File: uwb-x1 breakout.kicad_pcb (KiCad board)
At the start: 2 copper layers, 36.5 x 28 mm, 2 parts, among them J1 Conn_01x12, U1 UWB-X1-PRO

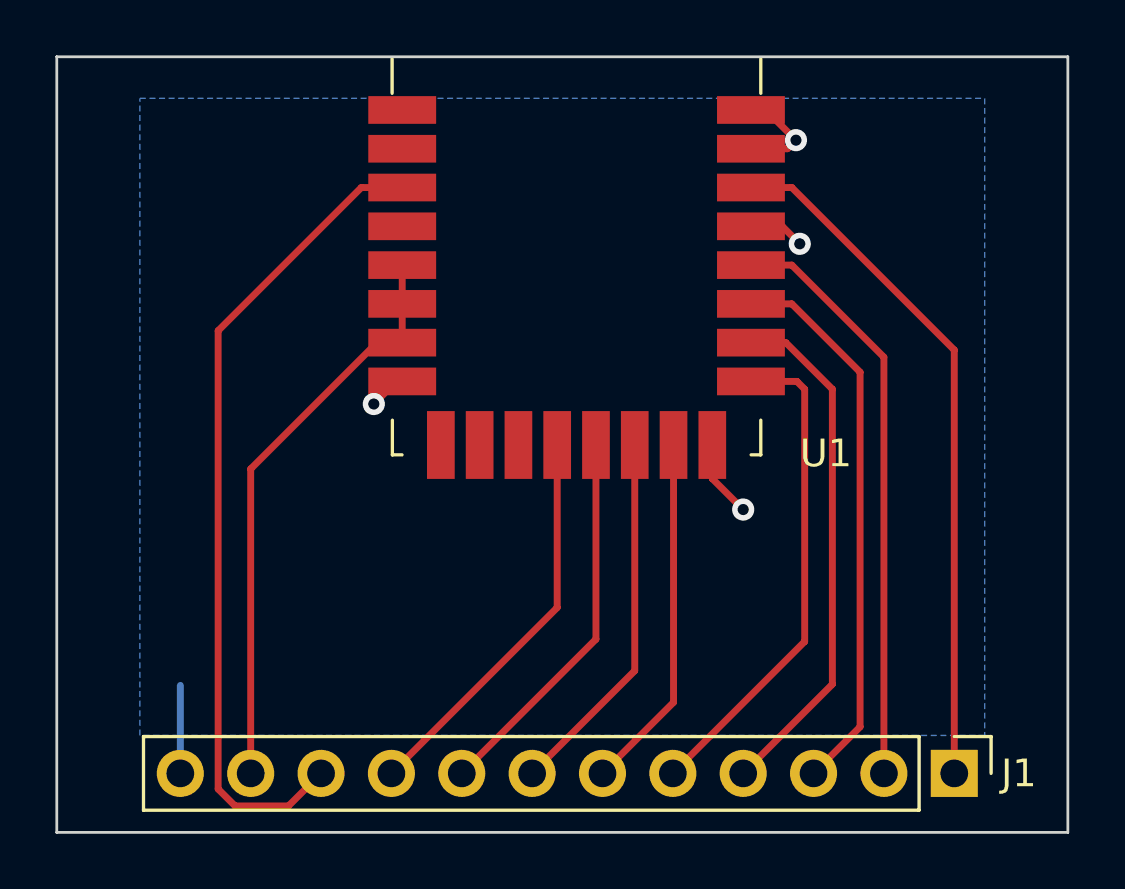
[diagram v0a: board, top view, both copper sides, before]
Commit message: Add silkscreen labels to pins
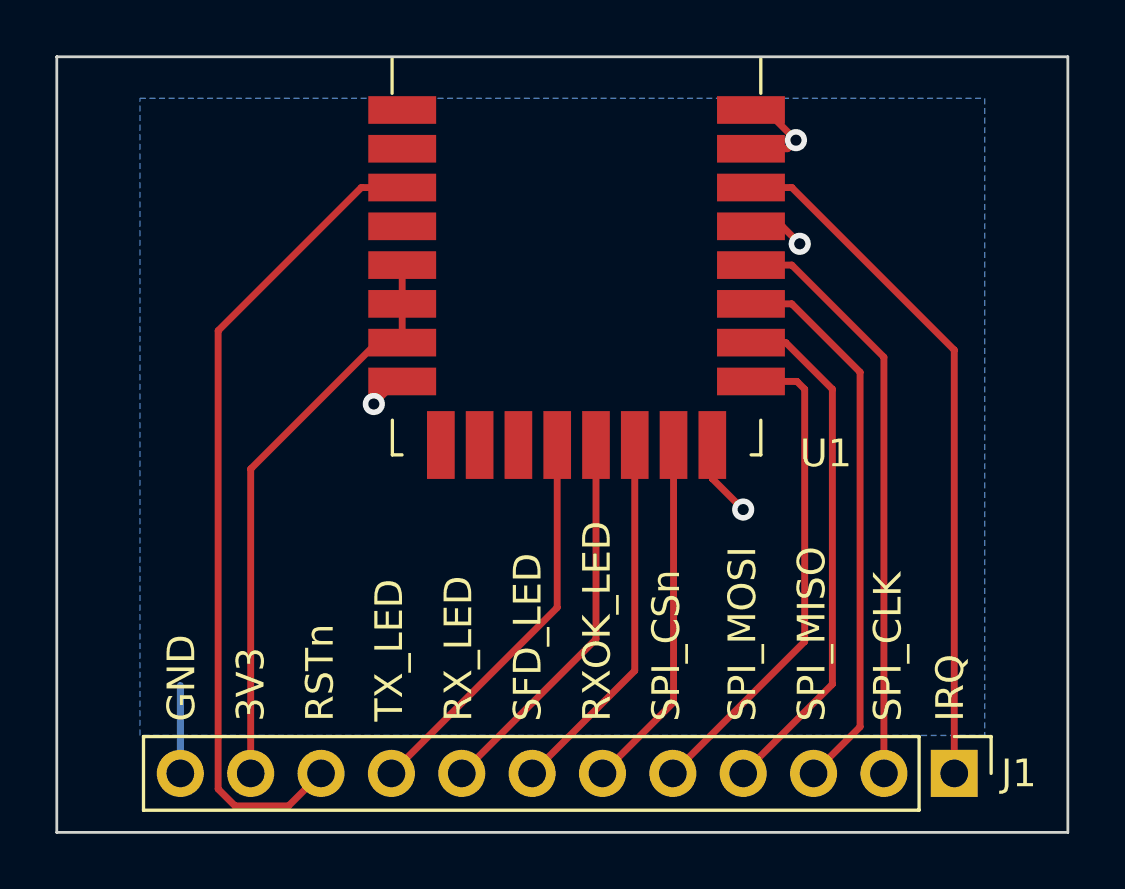
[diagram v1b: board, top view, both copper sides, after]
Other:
- board text added: "3V3"
- board text added: "GND"
- board text added: "IRQ"
- board text added: "RSTn"
- board text added: "RXOK_LED"
- board text added: "RX_LED"
- board text added: "SFD_LED"
- board text added: "SPI_CLK"
- board text added: "SPI_CSn"
- board text added: "SPI_MISO"
- board text added: "SPI_MOSI"
- board text added: "TX_LED"
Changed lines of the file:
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@@
   (general
     (thickness 1.6)
-    (drawings 4)
+    (drawings 16)
     (tracks 51)
     (zones 0)
@@
       (outputformat 1)
       (mirror false)
-      (drillshape 1)
+      (drillshape 0)
       (scaleselection 1)
-      (outputdirectory ""))
+      (outputdirectory "outputs/"))
   )
   (net 0 "")
@@
       (effects (font (size 1 1) (thickness 0.15)))
     )
+    (fp_line (start -0.635 -1.27) (end 1.27 -1.27) (layer F.Fab) (width 0.1))
+    (fp_line (start 1.27 -1.27) (end 1.27 29.21) (layer F.Fab) (width 0.1))
+    (fp_line (start 1.27 29.21) (end -1.27 29.21) (layer F.Fab) (width 0.1))
+    (fp_line (start -1.27 29.21) (end -1.27 -0.635) (layer F.Fab) (width 0.1))
+    (fp_line (start -1.27 -0.635) (end -0.635 -1.27) (layer F.Fab) (width 0.1))
+    (fp_line (start -1.33 29.27) (end 1.33 29.27) (layer F.SilkS) (width 0.12))
+    (fp_line (start -1.33 1.27) (end -1.33 29.27) (layer F.SilkS) (width 0.12))
+    (fp_line (start 1.33 1.27) (end 1.33 29.27) (layer F.SilkS) (width 0.12))
+    (fp_line (start -1.33 1.27) (end 1.33 1.27) (layer F.SilkS) (width 0.12))
+    (fp_line (start -1.33 0) (end -1.33 -1.33) (layer F.SilkS) (width 0.12))
+    (fp_line (start -1.33 -1.33) (end 0 -1.33) (layer F.SilkS) (width 0.12))
+    (fp_line (start -1.8 -1.8) (end -1.8 29.75) (layer F.CrtYd) (width 0.05))
+    (fp_line (start -1.8 29.75) (end 1.8 29.75) (layer F.CrtYd) (width 0.05))
+    (fp_line (start 1.8 29.75) (end 1.8 -1.8) (layer F.CrtYd) (width 0.05))
     (fp_line (start 1.8 -1.8) (end -1.8 -1.8) (layer F.CrtYd) (width 0.05))
-    (fp_line (start 1.8 29.75) (end 1.8 -1.8) (layer F.CrtYd) (width 0.05))
-    (fp_line (start -1.8 29.75) (end 1.8 29.75) (layer F.CrtYd) (width 0.05))
-    (fp_line (start -1.8 -1.8) (end -1.8 29.75) (layer F.CrtYd) (width 0.05))
-    (fp_line (start -1.33 -1.33) (end 0 -1.33) (layer F.SilkS) (width 0.12))
-    (fp_line (start -1.33 0) (end -1.33 -1.33) (layer F.SilkS) (width 0.12))
-    (fp_line (start -1.33 1.27) (end 1.33 1.27) (layer F.SilkS) (width 0.12))
-    (fp_line (start 1.33 1.27) (end 1.33 29.27) (layer F.SilkS) (width 0.12))
-    (fp_line (start -1.33 1.27) (end -1.33 29.27) (layer F.SilkS) (width 0.12))
-    (fp_line (start -1.33 29.27) (end 1.33 29.27) (layer F.SilkS) (width 0.12))
-    (fp_line (start -1.27 -0.635) (end -0.635 -1.27) (layer F.Fab) (width 0.1))
-    (fp_line (start -1.27 29.21) (end -1.27 -0.635) (layer F.Fab) (width 0.1))
-    (fp_line (start 1.27 29.21) (end -1.27 29.21) (layer F.Fab) (width 0.1))
-    (fp_line (start 1.27 -1.27) (end 1.27 29.21) (layer F.Fab) (width 0.1))
-    (fp_line (start -0.635 -1.27) (end 1.27 -1.27) (layer F.Fab) (width 0.1))
     (fp_text user %R (at 0 13.97) (layer F.Fab)
       (effects (font (size 1 1) (thickness 0.15)))
@@
       (effects (font (size 1 1) (thickness 0.15)))
     )
+    (fp_line (start -6.5 -5.525) (end -6.5 7.4) (layer F.Fab) (width 0.1))
+    (fp_line (start -6.5 7.4) (end 6.5 7.4) (layer F.Fab) (width 0.1))
+    (fp_line (start 6.5 7.4) (end 6.5 -5.525) (layer F.Fab) (width 0.1))
+    (fp_line (start -6.66 -6.75) (end -6.66 -5.5) (layer F.SilkS) (width 0.12))
+    (fp_line (start 6.65 -6.75) (end 6.65 -5.5) (layer F.SilkS) (width 0.12))
+    (fp_line (start -6.3 7.55) (end -6.65 7.55) (layer F.SilkS) (width 0.12))
+    (fp_line (start -6.65 7.55) (end -6.65 6.3) (layer F.SilkS) (width 0.12))
+    (fp_line (start 6.3 7.55) (end 6.65 7.55) (layer F.SilkS) (width 0.12))
+    (fp_line (start 6.65 7.55) (end 6.65 6.3) (layer F.SilkS) (width 0.12))
+    (fp_line (start 7.75 -5.525) (end 7.75 8.65) (layer F.CrtYd) (width 0.05))
+    (fp_line (start 7.75 8.65) (end -7.75 8.65) (layer F.CrtYd) (width 0.05))
+    (fp_line (start -7.75 8.65) (end -7.75 -5.525) (layer F.CrtYd) (width 0.05))
+    (fp_line (start -6.5 -5.525) (end 6.5 -5.525) (layer F.Fab) (width 0.1))
+    (fp_line (start -6.5 -5.525) (end -6.5 -15.6) (layer F.Fab) (width 0.1))
+    (fp_line (start 6.5 -5.525) (end 6.5 -15.6) (layer F.Fab) (width 0.1))
+    (fp_line (start -6.5 -15.6) (end 6.5 -15.6) (layer F.Fab) (width 0.12))
+    (fp_line (start -16.5 -5.525) (end -7.75 -5.525) (layer F.CrtYd) (width 0.05))
+    (fp_line (start 7.75 -5.525) (end 16.5 -5.525) (layer F.CrtYd) (width 0.05))
+    (fp_line (start 16.5 -5.525) (end 16.5 -15.6) (layer F.CrtYd) (width 0.05))
+    (fp_line (start 16.5 -15.6) (end -16.5 -15.6) (layer F.CrtYd) (width 0.05))
     (fp_line (start -16.5 -5.525) (end -16.5 -15.6) (layer F.CrtYd) (width 0.05))
-    (fp_line (start 16.5 -15.6) (end -16.5 -15.6) (layer F.CrtYd) (width 0.05))
-    (fp_line (start 16.5 -5.525) (end 16.5 -15.6) (layer F.CrtYd) (width 0.05))
-    (fp_line (start 7.75 -5.525) (end 16.5 -5.525) (layer F.CrtYd) (width 0.05))
-    (fp_line (start -16.5 -5.525) (end -7.75 -5.525) (layer F.CrtYd) (width 0.05))
-    (fp_line (start -6.5 -15.6) (end 6.5 -15.6) (layer F.Fab) (width 0.12))
-    (fp_line (start 6.5 -5.525) (end 6.5 -15.6) (layer F.Fab) (width 0.1))
-    (fp_line (start -6.5 -5.525) (end -6.5 -15.6) (layer F.Fab) (width 0.1))
-    (fp_line (start -6.5 -5.525) (end 6.5 -5.525) (layer F.Fab) (width 0.1))
-    (fp_line (start -7.75 8.65) (end -7.75 -5.525) (layer F.CrtYd) (width 0.05))
-    (fp_line (start 7.75 8.65) (end -7.75 8.65) (layer F.CrtYd) (width 0.05))
-    (fp_line (start 7.75 -5.525) (end 7.75 8.65) (layer F.CrtYd) (width 0.05))
-    (fp_line (start 6.65 7.55) (end 6.65 6.3) (layer F.SilkS) (width 0.12))
-    (fp_line (start 6.3 7.55) (end 6.65 7.55) (layer F.SilkS) (width 0.12))
-    (fp_line (start -6.65 7.55) (end -6.65 6.3) (layer F.SilkS) (width 0.12))
-    (fp_line (start -6.3 7.55) (end -6.65 7.55) (layer F.SilkS) (width 0.12))
-    (fp_line (start 6.65 -6.75) (end 6.65 -5.5) (layer F.SilkS) (width 0.12))
-    (fp_line (start -6.66 -6.75) (end -6.66 -5.5) (layer F.SilkS) (width 0.12))
-    (fp_line (start 6.5 7.4) (end 6.5 -5.525) (layer F.Fab) (width 0.1))
-    (fp_line (start -6.5 7.4) (end 6.5 7.4) (layer F.Fab) (width 0.1))
-    (fp_line (start -6.5 -5.525) (end -6.5 7.4) (layer F.Fab) (width 0.1))
     (fp_text user "10mm left and right" (at 0 -10.1) (layer Cmts.User)
       (effects (font (size 1 1) (thickness 0.15)))
@@
     (pad 1 smd rect (at -6.295 -4.9 90) (size 1 2.45) (layers F.Cu F.Paste F.Mask))
   )
+  (gr_text SPI_MOSI (at 144.75 101 90) (layer F.SilkS)
+    (effects (font (size 1 1) (thickness 0.15)) (justify left))
+  )
+  (gr_text IRQ (at 152.25 101 90) (layer F.SilkS)
+    (effects (font (size 1 1) (thickness 0.15)) (justify left))
+  )
+  (gr_text SPI_CLK (at 150 101 90) (layer F.SilkS)
+    (effects (font (size 1 1) (thickness 0.15)) (justify left))
+  )
+  (gr_text SPI_MISO (at 147.25 101 90) (layer F.SilkS)
+    (effects (font (size 1 1) (thickness 0.15)) (justify left))
+  )
+  (gr_text SPI_CSn (at 142 101 90) (layer F.SilkS)
+    (effects (font (size 1 1) (thickness 0.15)) (justify left))
+  )
+  (gr_text RXOK_LED (at 139.5 101 90) (layer F.SilkS)
+    (effects (font (size 1 1) (thickness 0.15)) (justify left))
+  )
+  (gr_text SFD_LED (at 137 101 90) (layer F.SilkS)
+    (effects (font (size 1 1) (thickness 0.15)) (justify left))
+  )
+  (gr_text RX_LED (at 134.5 101 90) (layer F.SilkS)
+    (effects (font (size 1 1) (thickness 0.15)) (justify left))
+  )
+  (gr_text TX_LED (at 132 101 90) (layer F.SilkS)
+    (effects (font (size 1 1) (thickness 0.15)) (justify left))
+  )
+  (gr_text RSTn (at 129.5 101 90) (layer F.SilkS)
+    (effects (font (size 1 1) (thickness 0.15)) (justify left))
+  )
+  (gr_text 3V3 (at 127 101 90) (layer F.SilkS)
+    (effects (font (size 1 1) (thickness 0.15)) (justify left))
+  )
+  (gr_text GND (at 124.5 101 90) (layer F.SilkS)
+    (effects (font (size 1 1) (thickness 0.15)) (justify left))
+  )
   (gr_line (start 156.5 77) (end 156.5 105) (layer Edge.Cuts) (width 0.1))
